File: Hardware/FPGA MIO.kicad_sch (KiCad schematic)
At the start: 24 parts, among them U3 XC7Z010-1CLG225I, U5 W25Q128JVS, U6 0473092651, X1 SIT8008BI-73-XXS-33.333333

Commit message: 11/17 progress update
finished the board, now just need to add the peripheral
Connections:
- net SDIO_D3: now reaches U3.A12 (PS_MIO52_501)
- net SDIO_D0: now reaches U3.A13 (PS_MIO38_501)
- net GPIO7: now reaches U3.A14 (PS_MIO35_501)
- net GPIO27: now reaches U3.B10 (PS_MIO11_500)
- net SDIO_D2: now reaches U3.B12 (PS_MIO48_501)
- net GPIO6: now reaches U3.B14 (PS_MIO36_501)
- net GPIO1: now reaches U3.B9 (PS_MIO14_500)
- net GPIO8: now reaches U3.C14 (PS_MIO37_501)
- net GPIO0: now reaches U3.D10 (PS_MIO15_500)
- net SDIO_D1: now reaches U3.D14 (PS_MIO39_501)
- net GPIO9: now reaches U3.D15 (PS_MIO34_501)
- net GPIO26: now reaches U3.D6 (PS_MIO10_500)

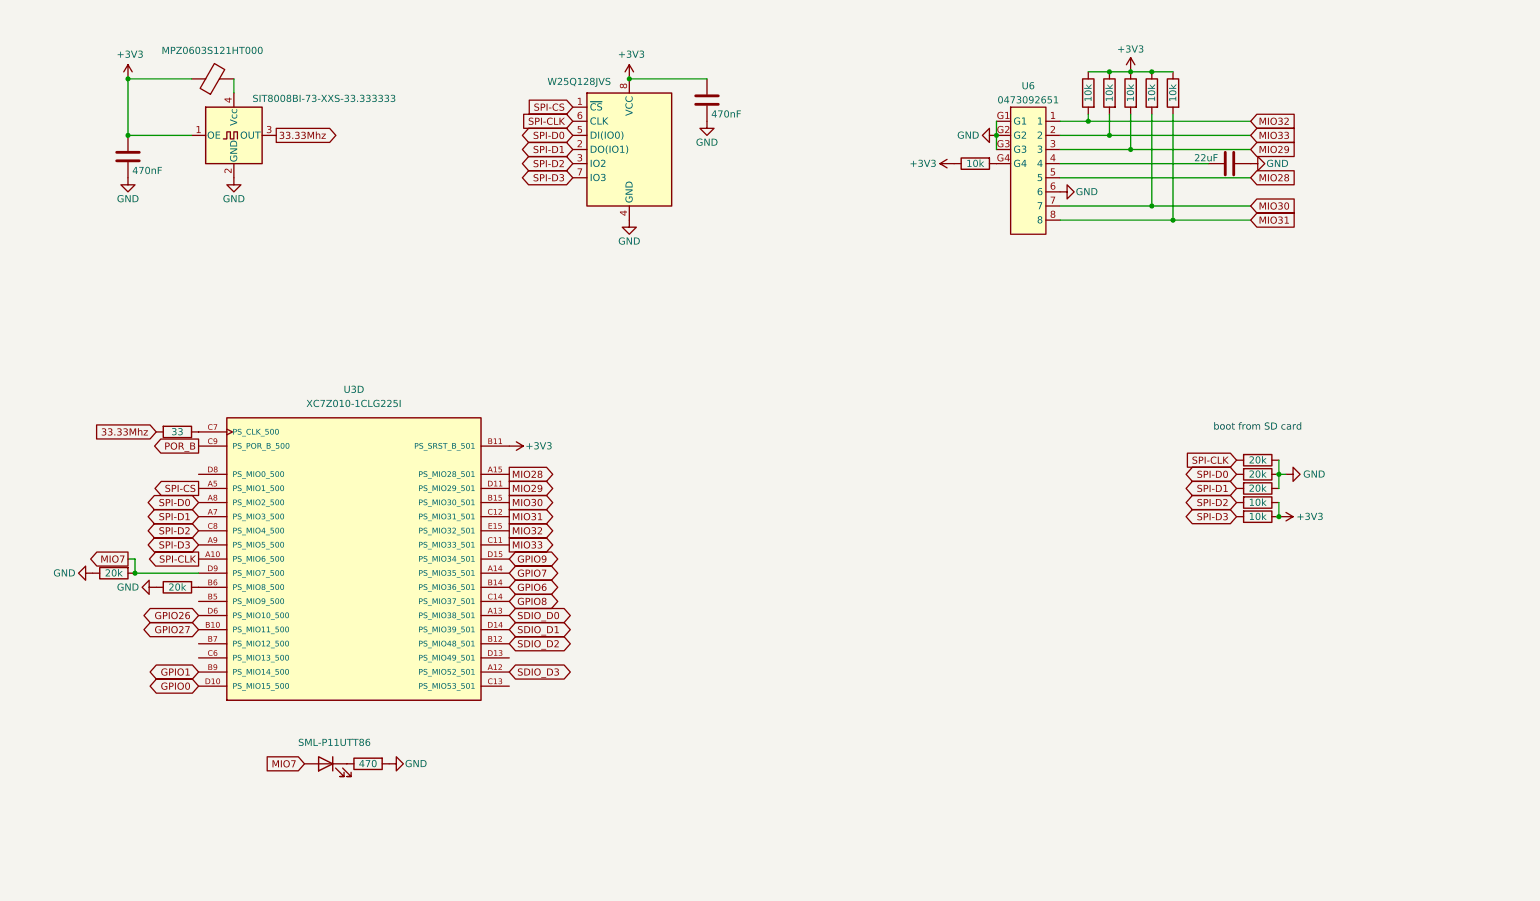
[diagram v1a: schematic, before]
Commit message: 11/19 update
add new header for jtag and fixed a couple of small things
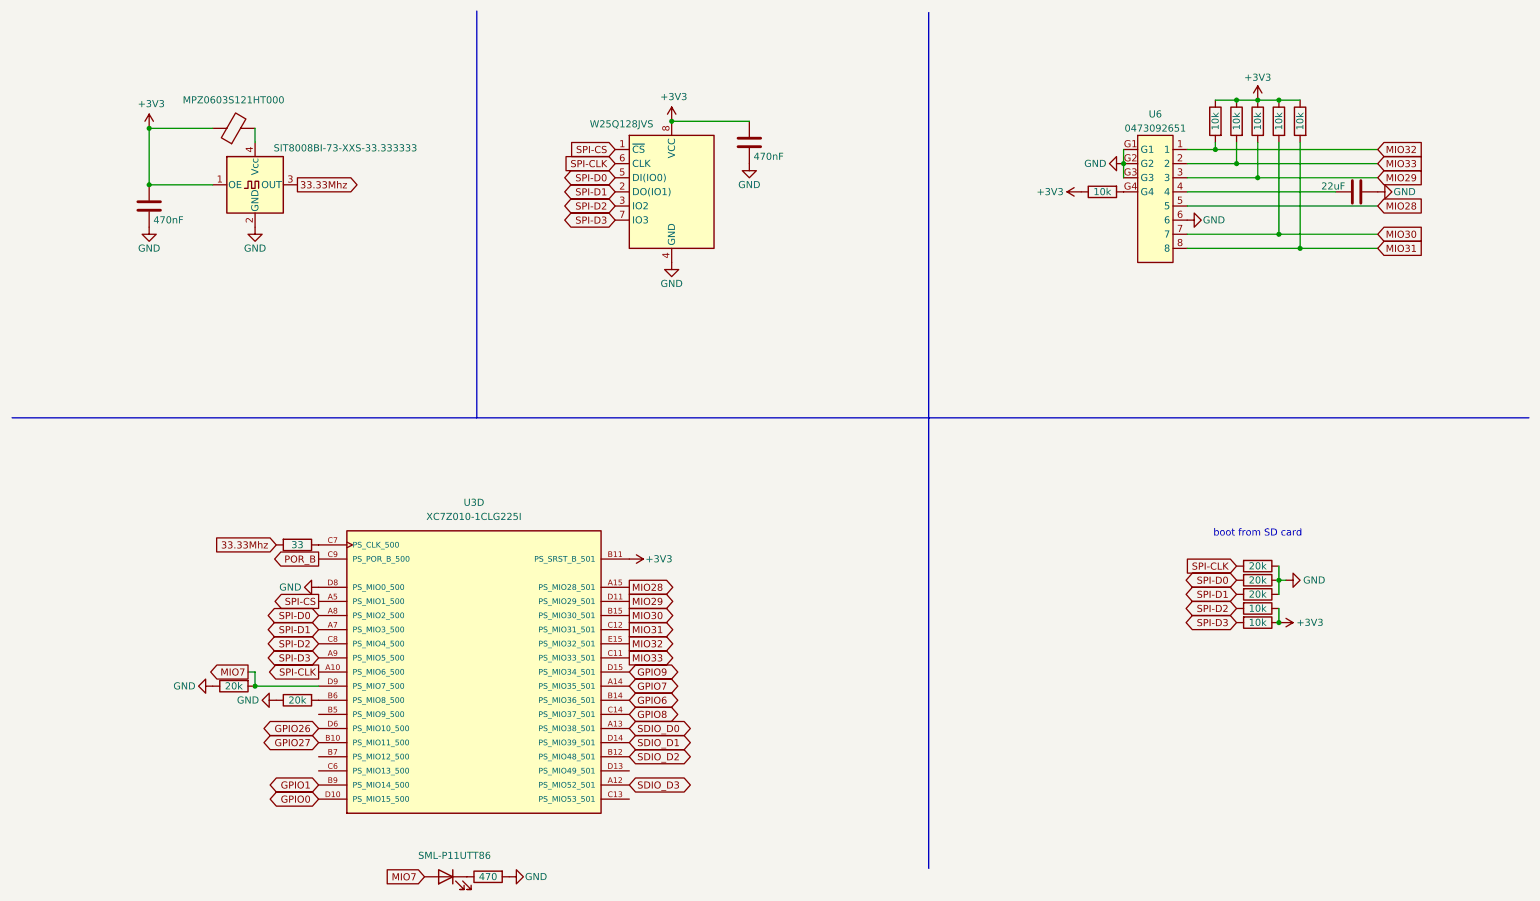
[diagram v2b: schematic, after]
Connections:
- net GND: now also U3.D8 (PS_MIO0_500)
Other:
- moved on the sheet: U3D, U6

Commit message: 11/21 update
finished annotating the schematic and add pictures and output the pdf
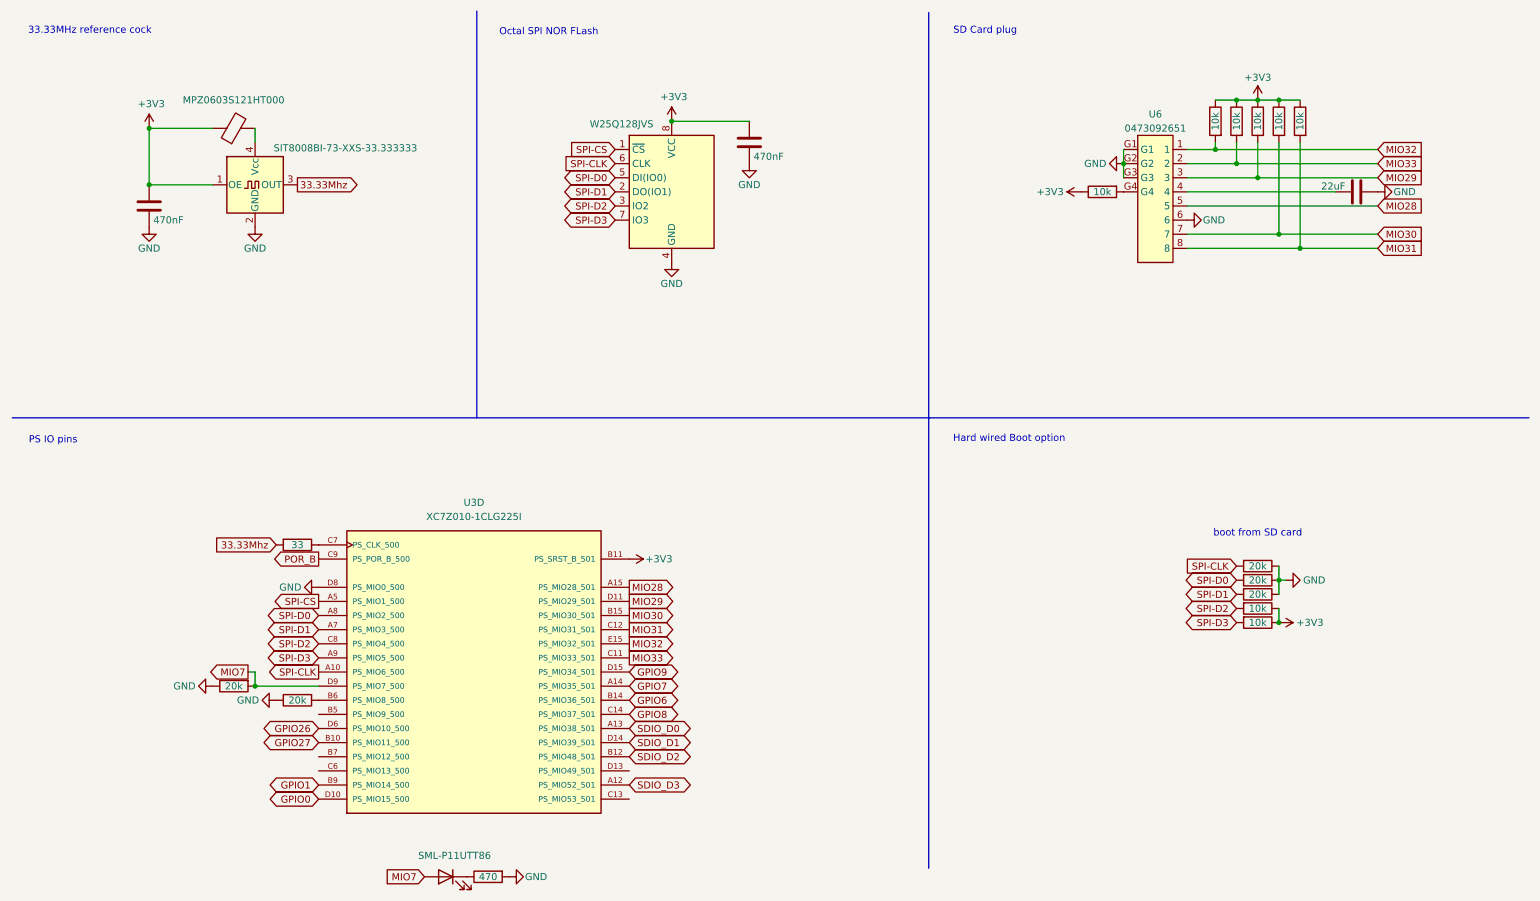
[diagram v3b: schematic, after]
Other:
- note added: "33.33MHz reference cock"
- note added: "Hard wired Boot option"
- note added: "Octal SPI NOR FLash"
- note added: "PS IO pins"
- note added: "SD Card plug"
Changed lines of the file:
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@@
+		)
+	)
+	(text "SD Card plug"
+		(exclude_from_sim no)
+		(at 187.198 15.494 0)
+		(effects
+			(font
+				(size 1.27 1.27)
+			)
+		)
+	)
+	(text "33.33MHz reference cock"
+		(exclude_from_sim no)
+		(at 26.162 15.494 0)
+		(effects
+			(font
+				(size 1.27 1.27)
+			)
+		)
+	)
+	(text "Octal SPI NOR FLash"
+		(exclude_from_sim no)
+		(at 108.712 15.748 0)
+		(effects
+			(font
+				(size 1.27 1.27)
+			)
+		)
+	)
+	(text "PS IO pins"
+		(exclude_from_sim no)
+		(at 19.558 89.154 0)
+		(effects
+			(font
+				(size 1.27 1.27)
+			)
+		)
+	)
+	(text "Hard wired Boot option"
+		(exclude_from_sim no)
+		(at 191.516 88.9 0)
+		(effects
+			(font
+				(size 1.27 1.27)
+			)
 		)
 	)
